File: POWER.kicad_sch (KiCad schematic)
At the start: 37 parts, among them IC1 MP1584EN, IC2 MP1584EN, J8 Conn_Jack-DC

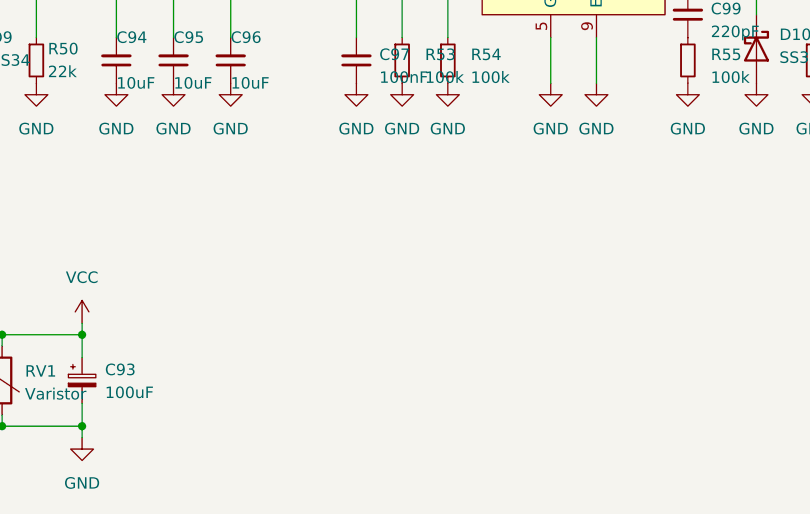
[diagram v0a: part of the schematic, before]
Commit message: Add power LED and some Silkscreen text.
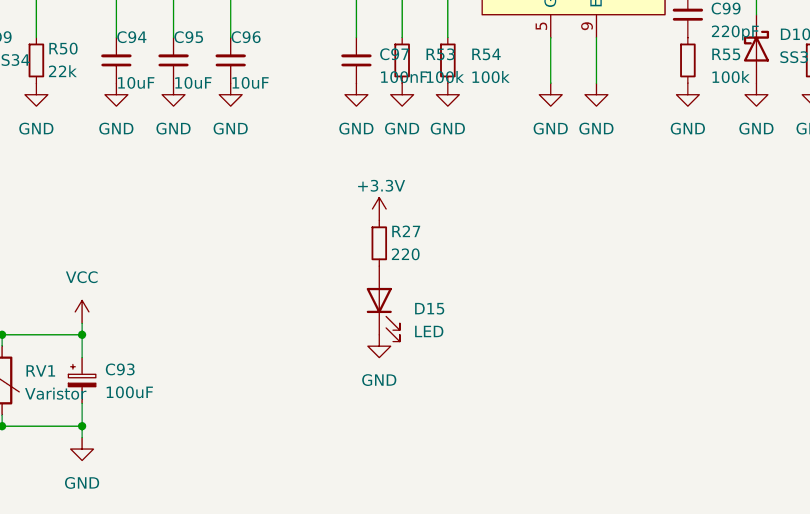
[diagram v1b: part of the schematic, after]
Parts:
- added D15: LED, Anh_Footprints:LED_0603, symbol Device:LED
- added R27: 220, Anh_Footprints:R_0603, symbol Device:R_Small
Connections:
- net +3.3V: now also R27.1
- net GND: now also D15.1 (K)
- new net: D15.2 (A), R27.2
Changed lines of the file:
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@@
+    )
+  )
+  (symbol (lib_id "power:GND") (at 114.3 93.98 0) (unit 1)
+    (in_bom yes) (on_board yes) (dnp no) (fields_autoplaced)
+    (property "Reference" "#PWR0188" (at 114.3 100.33 0)
+      (effects (font (size 1.27 1.27)) hide)
+    )
+    (property "Value" "GND" (at 114.3 99.06 0)
+      (effects (font (size 1.27 1.27)))
+    )
+    (property "Footprint" "" (at 114.3 93.98 0)
+      (effects (font (size 1.27 1.27)) hide)
+    )
+    (property "Datasheet" "" (at 114.3 93.98 0)
+      (effects (font (size 1.27 1.27)) hide)
+    )
+    (pin "1")
+    (instances
+      (project "GatewayPlus_V1.4"
+        (path "/6b25bb2e-e3f8-49e6-940a-fa3f985570a5/4931c4f2-ec98-49ed-98f1-a79587b46d92"
+          (reference "#PWR0188") (unit 1)
+        )
+      )
     )
   )
@@
     )
   )
+  (symbol (lib_id "Device:LED") (at 114.3 90.17 90) (unit 1)
+    (in_bom yes) (on_board yes) (dnp no) (fields_autoplaced)
+    (property "Reference" "D15" (at 118.11 91.1225 90)
+      (effects (font (size 1.27 1.27)) (justify right))
+    )
+    (property "Value" "LED" (at 118.11 93.6625 90)
+      (effects (font (size 1.27 1.27)) (justify right))
+    )
+    (property "Footprint" "Anh_Footprints:LED_0603" (at 114.3 90.17 0)
+      (effects (font (size 1.27 1.27)) hide)
+    )
+    (property "Datasheet" "~" (at 114.3 90.17 0)
+      (effects (font (size 1.27 1.27)) hide)
+    )
+    (pin "1")
+    (pin "2")
+    (instances
+      (project "GatewayPlus_V1.4"
+        (path "/6b25bb2e-e3f8-49e6-940a-fa3f985570a5/4931c4f2-ec98-49ed-98f1-a79587b46d92"
+          (reference "D15") (unit 1)
+        )
+      )
+    )
+  )
   (symbol (lib_id "Diode:CDBA340-HF") (at 156.21 62.23 270) (unit 1)
     (in_bom yes) (on_board yes) (dnp no) (fields_autoplaced)
@@
         (path "/6b25bb2e-e3f8-49e6-940a-fa3f985570a5/4931c4f2-ec98-49ed-98f1-a79587b46d92"
           (reference "C98") (unit 1)
+        )
+      )
+    )
+  )
+  (symbol (lib_id "Device:R_Small") (at 114.3 83.82 0) (unit 1)
+    (in_bom yes) (on_board yes) (dnp no)
+    (property "Reference" "R27" (at 115.57 82.55 0)
+      (effects (font (size 1.27 1.27)) (justify left))
+    )
+    (property "Value" "220" (at 115.57 85.09 0)
+      (effects (font (size 1.27 1.27)) (justify left))
+    )
+    (property "Footprint" "Anh_Footprints:R_0603" (at 114.3 83.82 0)
+      (effects (font (size 1.27 1.27)) hide)
+    )
+    (property "Datasheet" "~" (at 114.3 83.82 0)
+      (effects (font (size 1.27 1.27)) hide)
+    )
+    (pin "1")
+    (pin "2")
+    (instances
+      (project "GatewayPlus_V1.4"
+        (path "/6b25bb2e-e3f8-49e6-940a-fa3f985570a5/4931c4f2-ec98-49ed-98f1-a79587b46d92"
+          (reference "R27") (unit 1)
         )
       )
@@
         )
       )
+    )
+  )
+  (symbol (lib_id "power:+3.3V") (at 114.3 81.28 0) (unit 1)
+    (in_bom yes) (on_board yes) (dnp no)
+    (property "Reference" "#PWR0187" (at 114.3 85.09 0)
+      (effects (font (size 1.27 1.27)) hide)
+    )
+    (property "Value" "+3.3V" (at 111.76 77.47 0)
+      (effects (font (size 1.27 1.27)) (justify left))
+    )
+    (property "Footprint" "" (at 114.3 81.28 0)
+      (effects (font (size 1.27 1.27)) hide)
+    )
+    (property "Datasheet" "" (at 114.3 81.28 0)
+      (effects (font (size 1.27 1.27)) hide)
+    )
+    (pin "1")
+    (instances
+      (project "GatewayPlus_V1.4"
+        (path "/6b25bb2e-e3f8-49e6-940a-fa3f985570a5/4931c4f2-ec98-49ed-98f1-a79587b46d92"
+          (reference "#PWR0187") (unit 1)
+        )
+      )
